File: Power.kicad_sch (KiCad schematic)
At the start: 79 parts, among them J10 Conn_01x02_Socket, J12 USB_C_Receptacle_USB2.0_14P, J22 Conn_01x02_Socket, J23 Conn_01x02_Socket, J24 Conn_01x02_Socket, J25 Conn_01x02_Socket, Q1 NMOS, Q6 NMOS, Q7 NMOS, U10 INA219AxD, U12 USBLC6-2P6, U15 TPS60400DBV, U17 TCPP03-M20, U18 TPS54302, U4 TPS513885VABR, U9 INA219AxD

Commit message: shunts
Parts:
- removed R38, R39: 10k, Resistor_SMD:R_0603_1608Metric, symbol Device:R

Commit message: saving progress
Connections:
- net +3V3 is gone; now on net 3V3: U17.2 (VCC_{VCONN}), U4.6 (EN)
- net +5V renamed 5V_Buck
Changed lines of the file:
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@@
 	)
 	(junction
-		(at 293.37 100.33)
-		(diameter 0)
-		(color 0 0 0 0)
-	)
-	(junction
 		(at 218.44 168.91)
 		(diameter 0)
@@
 		)
 	)
+	(hierarchical_label "5V_Buck"
+		(shape input)
+		(at 293.37 100.33 0)
+		(effects
+			(font
+				(size 1.27 1.27)
+			)
+			(justify left)
+		)
+	)
 	(hierarchical_label "STM32_USB_D_N"
 		(shape input)
@@
 			)
 		)
-		(property "Value" "+3V3"
+		(property "Value" "3V3"
 			(at 255.778 171.958 0)
 			(show_name no)
@@
 			)
 		)
-		(property "Value" "+3V3"
-			(at 185.42 109.22 0)
+		(property "Value" "3V3"
+			(at 187.96 113.0299 0)
 			(show_name no)
 			(do_not_autoplace no)
@@
 					(size 1.27 1.27)
 				)
+				(justify left)
 			)
 		)
@@
 					(unit 1)
 				)
-			)
-		)
-	)
-	(symbol
-		(lib_id "power:+5V")
-		(at 293.37 100.33 0)
-		(unit 1)
-		(body_style 1)
-		(exclude_from_sim no)
-		(in_bom yes)
-		(on_board yes)
-		(in_pos_files yes)
-		(dnp no)
-		(fields_autoplaced yes)
-		(property "Reference" "#PWR016"
-			(at 293.37 104.14 0)
-			(hide yes)
-			(show_name no)
-			(do_not_autoplace no)
-			(effects
-				(font
-					(size 1.27 1.27)
-				)
-			)
-		)
-		(property "Value" "+5V"
-			(at 293.37 95.25 0)
-			(show_name no)
-			(do_not_autoplace no)
-			(effects
-				(font
-					(size 1.27 1.27)
-				)
-			)
-		)
-		(property "Footprint" ""
-			(at 293.37 100.33 0)
-			(hide yes)
-			(show_name no)
-			(do_not_autoplace no)
-			(effects
-				(font
-					(size 1.27 1.27)
-				)
-			)
-		)
-		(property "Datasheet" ""
-			(at 293.37 100.33 0)
-			(hide yes)
-			(show_name no)
-			(do_not_autoplace no)
-			(effects
-				(font
-					(size 1.27 1.27)
-				)
-			)
-		)
-		(property "Description" "Power symbol creates a global label with name \"+5V\""
-			(at 293.37 100.33 0)
-			(hide yes)
-			(show_name no)
-			(do_not_autoplace no)
-			(effects
-				(font
-					(size 1.27 1.27)
-				)
-			)
-		)
-		(pin "1"
-		)
-		(instances
-			(project "SeniorDesign_PCB"
-				(path "/88e1ced0-9576-4565-ab29-f74bf51ccbda/ab582717-e2bf-4603-b10c-c3fa663dfded"
-					(reference "#PWR016")
-					(unit 1)
-				)

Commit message: Buck routing, general routing / placement, edgecuts and planes
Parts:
- C78: footprint Package_TO_SOT_SMD:SOT-23-6 -> Capacitor_SMD:C_0603_1608Metric_Pad1.08x0.95mm_HandSolder
- R86, R88: footprint Resistor_SMD:R_1210_3225Metric_Pad1.30x2.65mm_HandSolder -> Resistor_SMD:R_0805_2012Metric
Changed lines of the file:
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@@
 			)
 		)
-		(property "Footprint" "Package_TO_SOT_SMD:SOT-23-6"
+		(property "Footprint" "Capacitor_SMD:C_0603_1608Metric_Pad1.08x0.95mm_HandSolder"
 			(at 148.2852 46.99 0)
 			(hide yes)
@@
 			)
 		)
-		(property "Footprint" "Resistor_SMD:R_1210_3225Metric_Pad1.30x2.65mm_HandSolder"
+		(property "Footprint" "Resistor_SMD:R_0805_2012Metric"
 			(at 130.81 39.878 90)
 			(hide yes)
@@
 			)
 		)
-		(property "Footprint" "Resistor_SMD:R_1210_3225Metric_Pad1.30x2.65mm_HandSolder"
+		(property "Footprint" "Resistor_SMD:R_0805_2012Metric"
 			(at 130.81 33.528 90)
 			(hide yes)

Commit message: working on buck
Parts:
- C78: footprint Capacitor_SMD:C_0603_1608Metric_Pad1.08x0.95mm_HandSolder -> Package_TO_SOT_SMD:SOT-23-6
- R86, R88: footprint Resistor_SMD:R_0805_2012Metric -> Resistor_SMD:R_1210_3225Metric_Pad1.30x2.65mm_HandSolder
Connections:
- net 3V3: now also U12.5 (VBUS)
- net VBUS_STM: no longer U12.5 (VBUS)
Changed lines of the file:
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@@
 	)
 	(junction
-		(at 176.53 168.91)
-		(diameter 0)
-		(color 0 0 0 0)
-	)
-	(junction
 		(at 160.02 120.65)
 		(diameter 0)
@@
 	(wire
 		(pts
-			(xy 176.53 168.91) (xy 176.53 179.07)
-		)
-		(stroke
-			(width 0)
-			(type default)
-		)
-	)
-	(wire
-		(pts
 			(xy 238.76 105.41) (xy 238.76 100.33)
 		)
@@
 			)
 		)
-		(property "Footprint" "Capacitor_SMD:C_0603_1608Metric_Pad1.08x0.95mm_HandSolder"
+		(property "Footprint" "Package_TO_SOT_SMD:SOT-23-6"
 			(at 148.2852 46.99 0)
 			(hide yes)
@@
 			)
 		)
-		(property "Footprint" "Resistor_SMD:R_0805_2012Metric"
+		(property "Footprint" "Resistor_SMD:R_1210_3225Metric_Pad1.30x2.65mm_HandSolder"
 			(at 130.81 39.878 90)
 			(hide yes)
@@
 			)
 		)
-		(property "Footprint" "Resistor_SMD:R_0805_2012Metric"
+		(property "Footprint" "Resistor_SMD:R_1210_3225Metric_Pad1.30x2.65mm_HandSolder"
 			(at 130.81 33.528 90)
 			(hide yes)
@@
 					(unit 1)
 				)
+			)
+		)
+	)
+	(symbol
+		(lib_id "power:+3V3")
+		(at 176.53 179.07 0)
+		(unit 1)
+		(body_style 1)
+		(exclude_from_sim no)
+		(in_bom yes)
+		(on_board yes)
+		(in_pos_files yes)
+		(dnp no)
+		(property "Reference" "#PWR074"
+			(at 176.53 182.88 0)
+			(hide yes)
+			(show_name no)
+			(do_not_autoplace no)
+			(effects
+				(font
+					(size 1.27 1.27)
+				)
+			)
+		)
+		(property "Value" "3V3"
+			(at 173.228 177.038 0)
+			(show_name no)
+			(do_not_autoplace no)
+			(effects
+				(font
+					(size 1.27 1.27)
+				)
+			)
+		)
+		(property "Footprint" ""
+			(at 176.53 179.07 0)
+			(hide yes)
+			(show_name no)
+			(do_not_autoplace no)
+			(effects
+				(font
+					(size 1.27 1.27)
+				)
+			)
+		)
+		(property "Datasheet" ""
+			(at 176.53 179.07 0)
+			(hide yes)
+			(show_name no)
+			(do_not_autoplace no)
+			(effects
+				(font
+					(size 1.27 1.27)
+				)
+			)
+		)
+		(property "Description" "Power symbol creates a global label with name \"+3V3\""
+			(at 176.53 179.07 0)
+			(hide yes)
+			(show_name no)
+			(do_not_autoplace no)
+			(effects
+				(font
+					(size 1.27 1.27)
+				)
+			)
+		)
+		(pin "1"
+		)
+		(instances
+			(project "SeniorDesign_PCB"
+				(path "/88e1ced0-9576-4565-ab29-f74bf51ccbda/ab582717-e2bf-4603-b10c-c3fa663dfded"
+					(reference "#PWR074")
+					(unit 1)
+				)

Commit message: second buck
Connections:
- net +20V is gone; now on net 20V: J25.1 (Pin_1)
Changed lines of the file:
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@@
 			)
 		)
-		(property "Value" "+20V"
+		(property "Value" "20V"
 			(at 365.76 70.104 0)
 			(show_name no)

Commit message: Matrix routing plus pwr
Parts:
- removed D4: SMAJ5.0A, Diode_SMD:D_SMA, symbol Diode:SMAJ5.0A
- removed F1: RGEF1400, Fuse:Fuseholder_Clip-5x20mm_Keystone_3512P_Inline_P23.62x7.27mm_D1.02x2.41x1.02x1.57mm_Horizontal, symbol Device:Polyfuse
- removed J24: Conn_01x02_Socket, Connector_Phoenix_SPT:PhoenixContact_SPT_2.5_2-H-5.0_1x02_P5.0mm_Horizontal, symbol Connector:Conn_01x02_Socket
- removed R33: 2m, Resistor_SMD:R_1206_3216Metric, symbol Device:R
- added C51: 1u, Capacitor_SMD:C_0603_1608Metric, symbol Device:C
- added C54: 100n, Capacitor_SMD:C_0603_1608Metric, symbol Device:C
- added D10: D, Diode_SMD:D_1206_3216Metric_Pad1.42x1.75mm_HandSolder, symbol Device:D
- added F2: RGEF1400, Fuse:Fuseholder_Clip-5x20mm_Keystone_3512P_Inline_P23.62x7.27mm_D1.02x2.41x1.02x1.57mm_Horizontal, symbol Device:Polyfuse
- added R38: 2m, Resistor_SMD:R_1206_3216Metric, symbol Device:R
- added R89: 0R, Resistor_SMD:R_1210_3225Metric_Pad1.30x2.65mm_HandSolder, symbol Device:R
- C78: footprint Package_TO_SOT_SMD:SOT-23-6 -> Capacitor_SMD:C_0603_1608Metric_Pad1.08x0.95mm_HandSolder
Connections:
- net 5V: now also D10.1 (K), R89.1; no longer J10.2 (Pin_2), U9.7 (IN-)
- net 5V_AMPS_1: now also F2.2, R38.1
- net GND: now also C51.2, C54.2
- net at C72.1, C77.1, C78.1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: now also R89.2
- net 5V_Buck: no longer names the net of C31.2, C56.1, L10.2, R63.1
- net 5V_Buck: now also F2.1
- new net 5V_AMPS_2: C51.1, C54.1, D10.2 (A), J10.2 (Pin_2), R38.2, U9.7 (IN-)
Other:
- note removed: "5V INPUT + PROTECTION"
- moved on the sheet: C18, C19, J10, Q1, R31, R32, R68, R69, R70, R71, R72, R73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

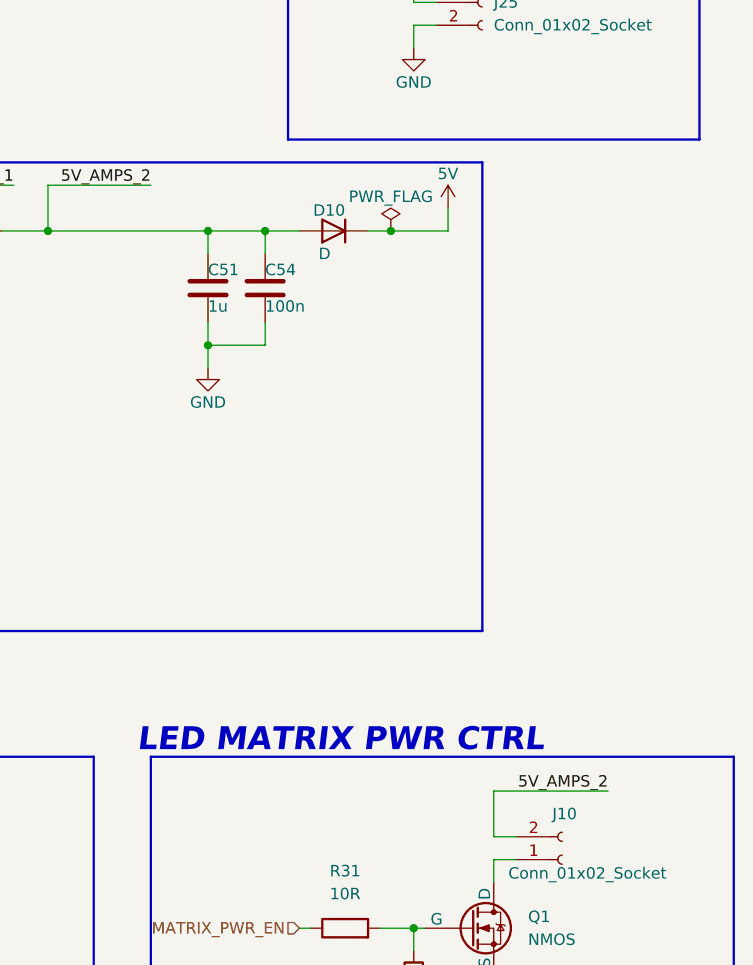
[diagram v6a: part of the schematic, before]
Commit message: 5V fix
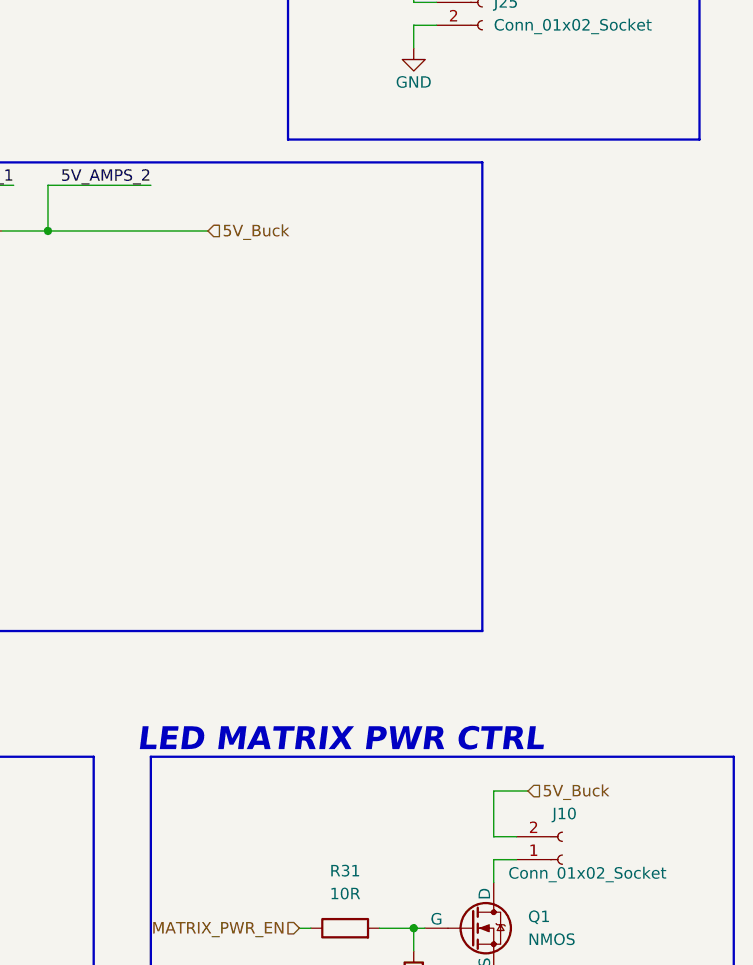
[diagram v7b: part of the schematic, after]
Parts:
- removed C51: 1u, Capacitor_SMD:C_0603_1608Metric, symbol Device:C
- removed C54: 100n, Capacitor_SMD:C_0603_1608Metric, symbol Device:C
- removed D10: D, Diode_SMD:D_1206_3216Metric_Pad1.42x1.75mm_HandSolder, symbol Device:D
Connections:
- net 5V_AMPS_2 renamed 5V_Buck

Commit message: keep on digging
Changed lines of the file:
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@@
-	)
-	(junction
-		(at 325.12 100.33)
-		(diameter 0)
-		(color 0 0 0 0)
 	)
 	(junction
@@
 	(wire
 		(pts
-			(xy 325.12 95.25) (xy 325.12 100.33)
-		)
-		(stroke
-			(width 0)
-			(type default)
-		)
-	)
-	(wire
-		(pts
 			(xy 278.13 100.33) (xy 256.54 100.33)
 		)
@@
 	(wire
 		(pts
-			(xy 320.04 100.33) (xy 325.12 100.33)
-		)
-		(stroke
-			(width 0)
-			(type default)
-		)
-	)
-	(wire
-		(pts
 			(xy 361.95 177.8) (xy 365.76 177.8)
 		)
@@
 	(wire
 		(pts
-			(xy 325.12 100.33) (xy 342.9 100.33)
+			(xy 320.04 100.33) (xy 342.9 100.33)
 		)
 		(stroke
@@
 	(wire
 		(pts
-			(xy 325.12 95.25) (xy 336.55 95.25)
-		)
-		(stroke
-			(width 0)
-			(type default)
-		)
-	)
-	(wire
-		(pts
 			(xy 143.51 184.15) (xy 144.78 184.15)
 		)
@@
 	(wire
 		(pts
-			(xy 24.13 45.72) (xy 39.37 45.72)
+			(xy 33.02 45.72) (xy 39.37 45.72)
 		)
 		(stroke
@@
 		)
 	)
-	(label "5V_AMPS_2"
-		(at 336.55 95.25 180)
-		(effects
-			(font
-				(size 1.27 1.27)
-			)
-			(justify right bottom)
-		)
-	)
 	(label "VBUS_STM"
 		(at 114.3 45.72 0)
@@
 		)
 	)
-	(label "5V_AMPS_2"
-		(at 24.13 45.72 0)
-		(effects
-			(font
-				(size 1.27 1.27)
-			)
-			(justify left bottom)
-		)
-	)
 	(label "3V3_AMPS_1"
 		(at 242.57 36.83 180)
@@
 		)
 	)
+	(hierarchical_label "5V_Buck"
+		(shape input)
+		(at 33.02 45.72 180)
+		(effects
+			(font
+				(size 1.27 1.27)
+			)
+			(justify right)
+		)
+	)
